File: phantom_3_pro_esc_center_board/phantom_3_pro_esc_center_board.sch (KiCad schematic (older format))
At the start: 138 parts, among them J1 CONN_BAT, J10 M1_BK, J11 M1_RD, J12 M1_YW, J13 M2_YW, J14 M2_RD, J15 M2_BK, J16 M3_BK, J17 M3_RD, J18 M3_YW, J19 M4_YW, J2 CONN_GPS, J20 M4_RD, J21 M4_BK, J3 CONN_GIMBAL, J4 CONN_CMPAS, J5 CONN_OFDM, J6 CONN_USB, J7 CONN_API, J8 CONN_MC_FRONT, J9 CONN_MC_BACK

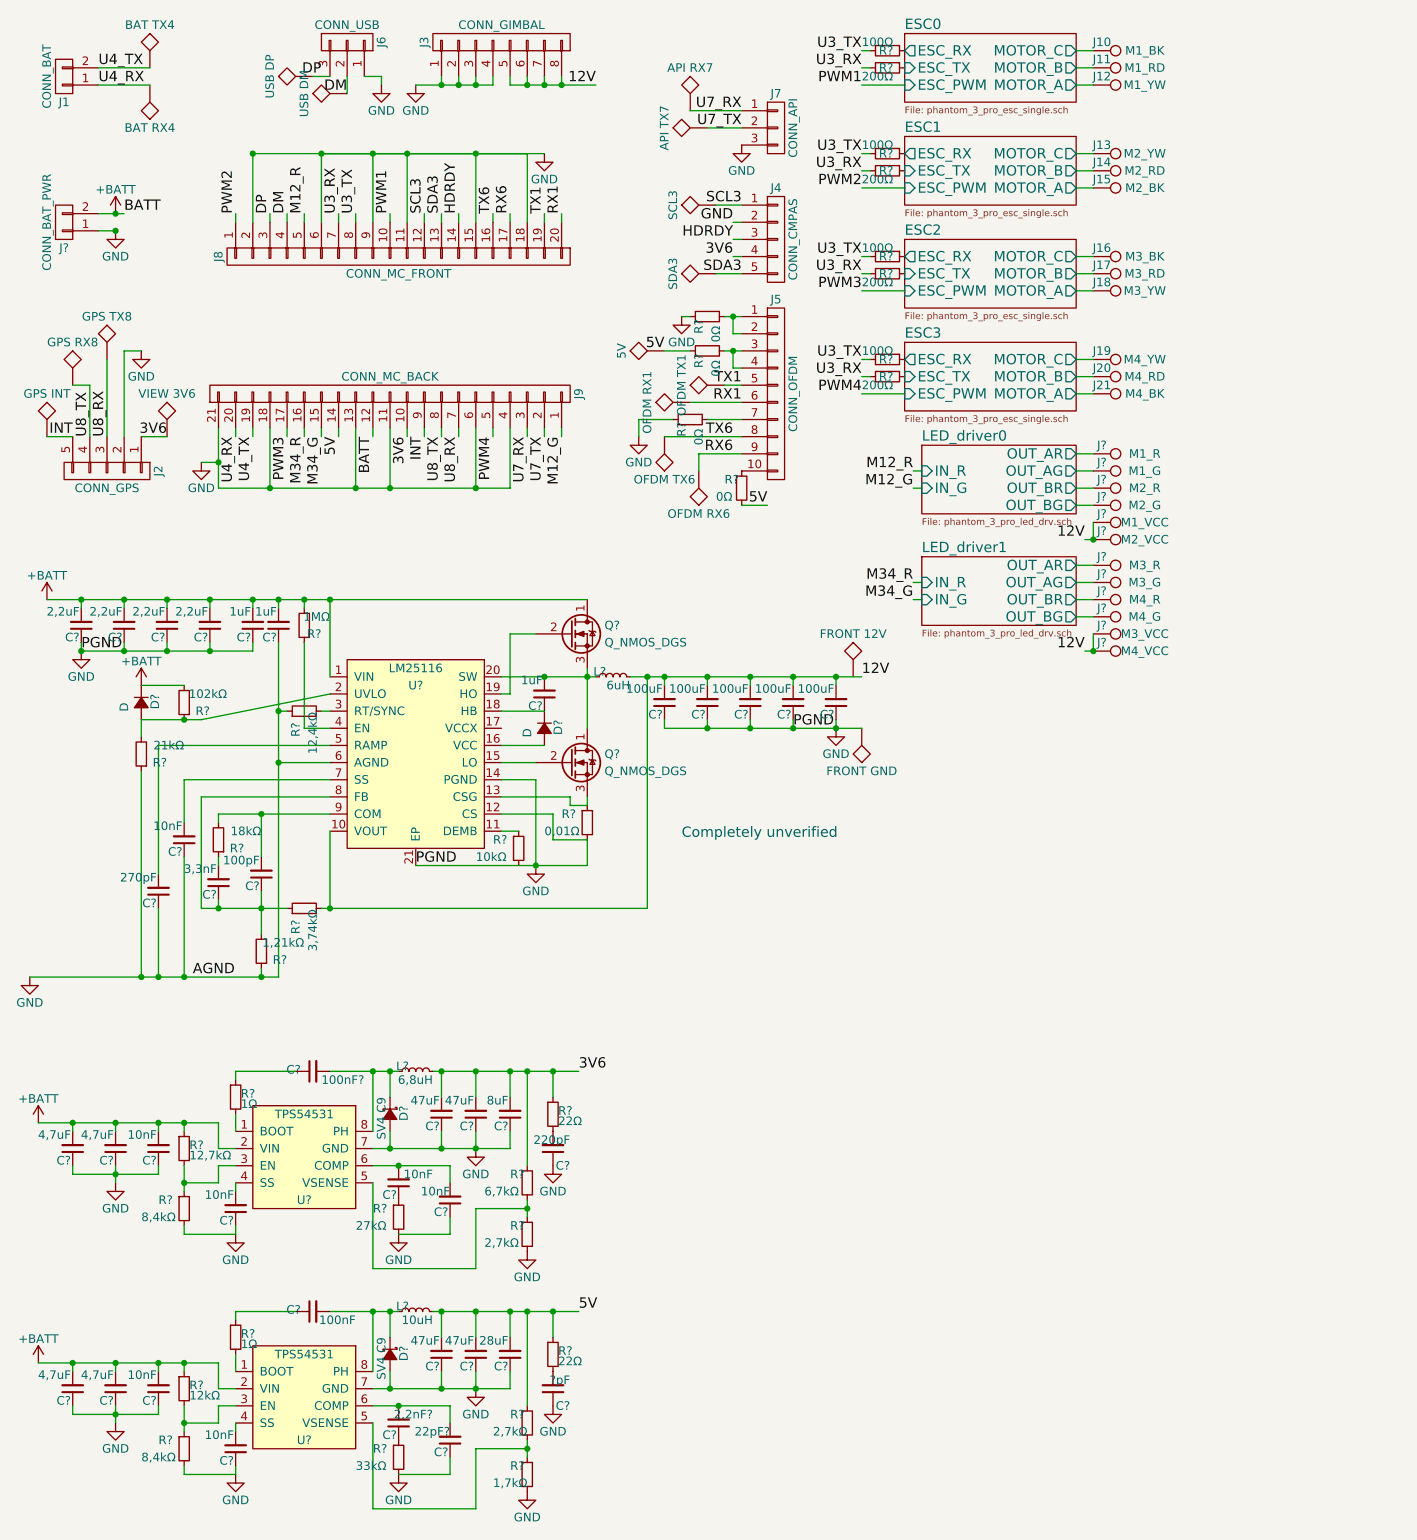
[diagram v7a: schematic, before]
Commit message: ESC Center: Formed a link between schematic and PCB.
Modified PCB to link some components to schematic.

Also created edge pad connectors to FC board.
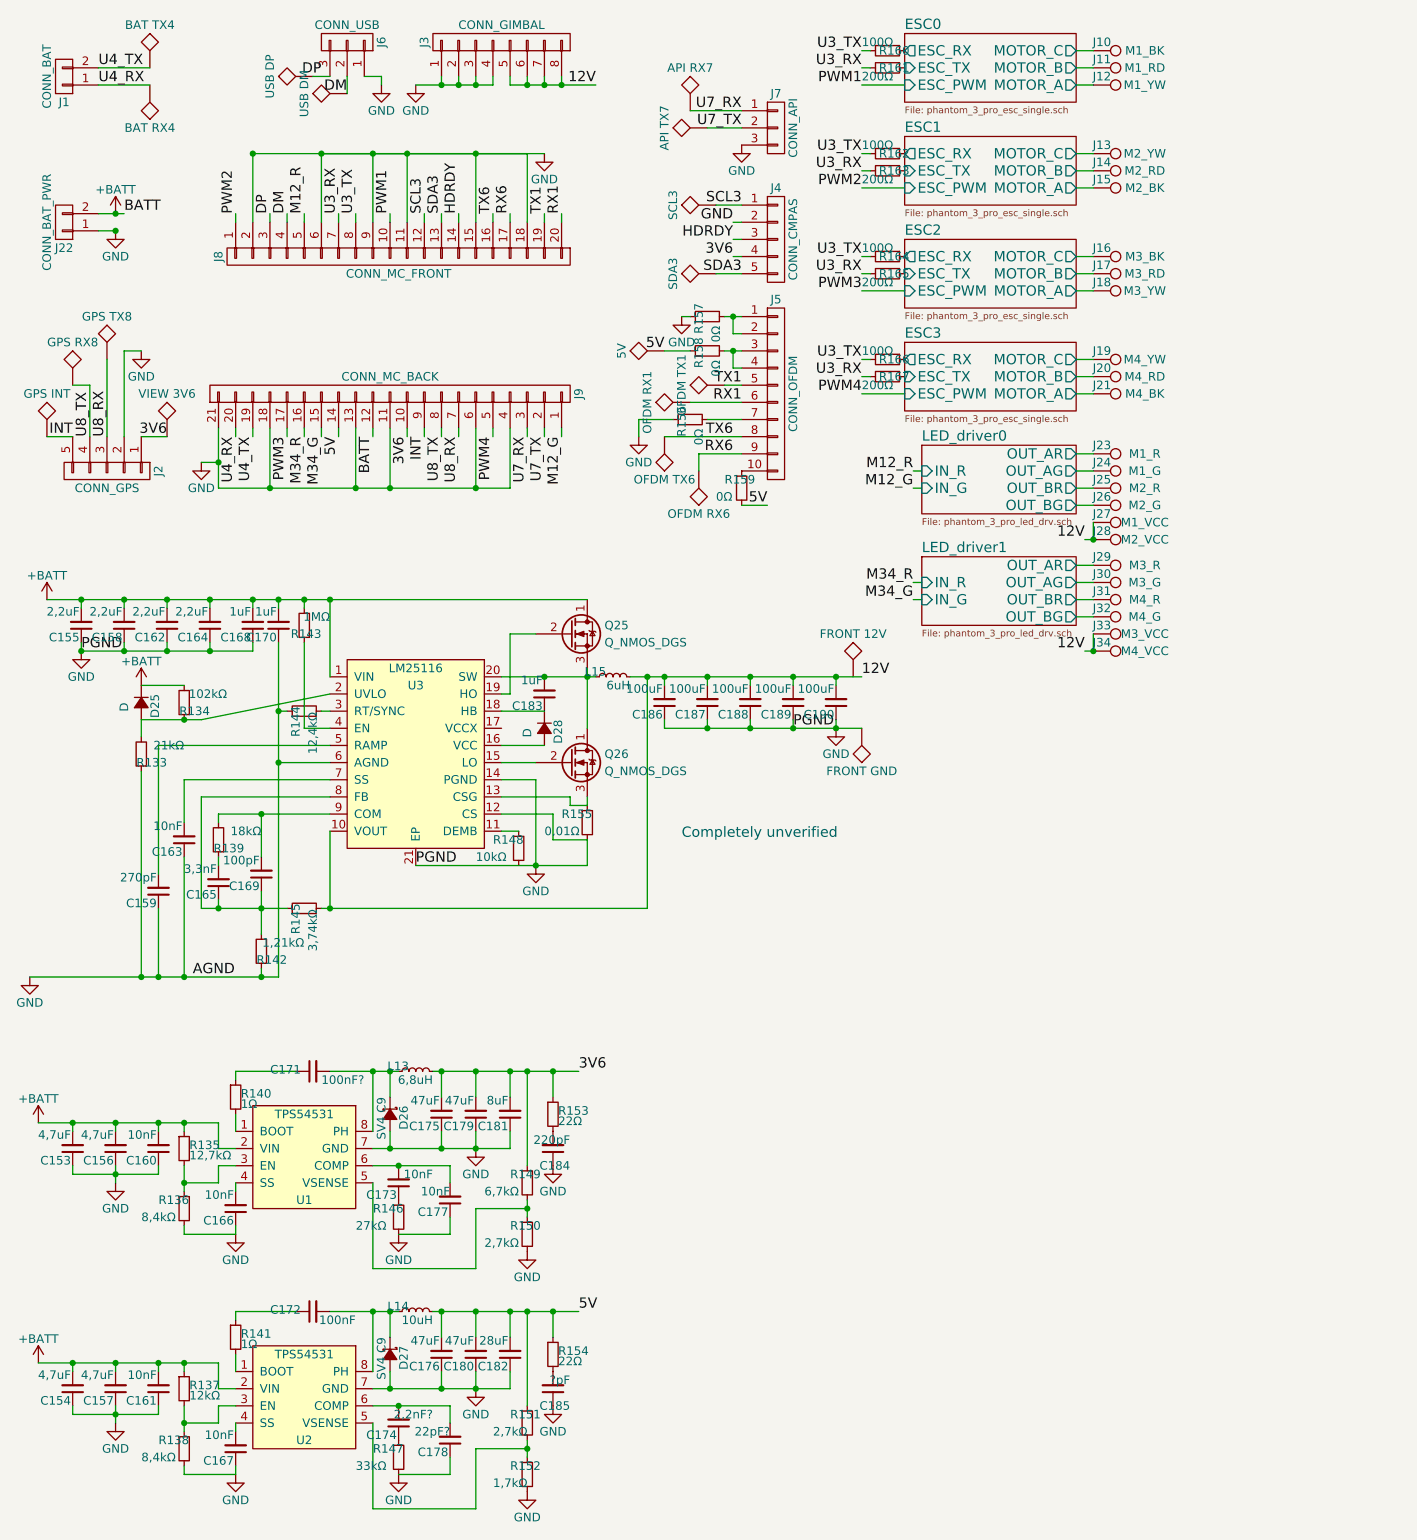
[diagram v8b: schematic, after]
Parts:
- removed TP?: GPS TX8, symbol TEST
- removed TP?: BAT TX4, symbol TEST
- removed TP?: BAT RX4, symbol TEST
- removed TP?: VIEW 3V6, symbol TEST
- removed TP?: USB DP, symbol TEST
- removed TP?: USB DM, symbol TEST
- removed TP?: 5V, symbol TEST
- removed TP?: API RX7, symbol TEST
- removed TP?: OFDM RX1, symbol TEST
- removed TP?: OFDM RX6, symbol TEST
- removed TP?: API TX7, symbol TEST
- removed TP?: SCL3, symbol TEST
- removed TP?: SDA3, symbol TEST
- removed TP?: OFDM TX1, symbol TEST
- removed TP?: FRONT 12V, symbol TEST
- removed TP?: FRONT GND, symbol TEST
- removed TP?: GPS RX8, symbol TEST
- added TP54: GPS RX8, symbol TEST
- added TP55: GPS TX8, symbol TEST
- added TP56: BAT TX4, symbol TEST
- added TP57: BAT RX4, symbol TEST
- added TP58: VIEW 3V6, symbol TEST
- added TP59: USB DP, symbol TEST
- added TP60: USB DM, symbol TEST
- added TP61: 5V, symbol TEST
- added TP63: API RX7, symbol TEST
- added TP64: OFDM RX1, symbol TEST
- added TP65: OFDM RX6, symbol TEST
- added TP66: API TX7, symbol TEST
- added TP67: SCL3, symbol TEST
- added TP68: SDA3, symbol TEST
- added TP69: OFDM TX1, symbol TEST
- added TP70: FRONT 12V, symbol TEST
- added TP71: FRONT GND, symbol TEST
- C153, C154, C155, C156, C157, C158, C159, C160, C161, C162, C163, C164, C165, C166, C168, C169, C170, C171, C173, C174, C175, C176, C177, C178, C179, C180, C181, C182, C183, C184, C185, C186, C187, C188, C189, C190: renamed from C?; footprint (none) -> Capacitors_SMD:C_0201
- C167: renamed from C?; footprint meas 9.3nF -> Capacitors_SMD:C_0201
- C172: renamed from C?; footprint meas. 96nF -> Capacitors_SMD:C_0201
- J8: footprint (none) -> Connectors_custom:Connector-edge-20pin-1.78mm
- J9: footprint (none) -> Connectors_custom:Connector-edge-21pin-1.78mm
- gave numbers to parts that had none: 62
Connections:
- net 3V6: now also TP58.1
- net 5V: now also TP61.1
- net DM: now also TP60.1
- net DP: now also TP59.1
- net GND: now also TP71.1
- net RX1: now also TP64.1
- net RX6: now also TP65.1
- net SCL3: now also TP67.1
- net SDA3: now also TP68.1
- net TX1: now also TP69.1
- net U4_RX: now also TP57.1
- net U4_TX: now also TP56.1
- net U7_RX: now also TP63.1
- net U7_TX: now also TP66.1
- net U8_RX: now also TP55.1
- net U8_TX: now also TP54.1
